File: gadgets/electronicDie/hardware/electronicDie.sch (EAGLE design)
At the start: 32 parts, among them IC1 CD4029N, IC2 NE555N, T1 BC327, T2 BC337, X1 USBPCB

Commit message: Add SMD power LED for testing purposes
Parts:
- added LED8: green, led:LEDCHIPLED_0603
- added R11: 1k, rcl_upravena:R-EU_R0603
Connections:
- new net N$3: LED8.A, R11.1
- net +5V: now also R11.2
- net GND: now also LED8.C
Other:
- moved on the sheet: C1, C2, C3, C4, D1, D2, D3, IC1, IC1P, IC2, LED1, LED2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

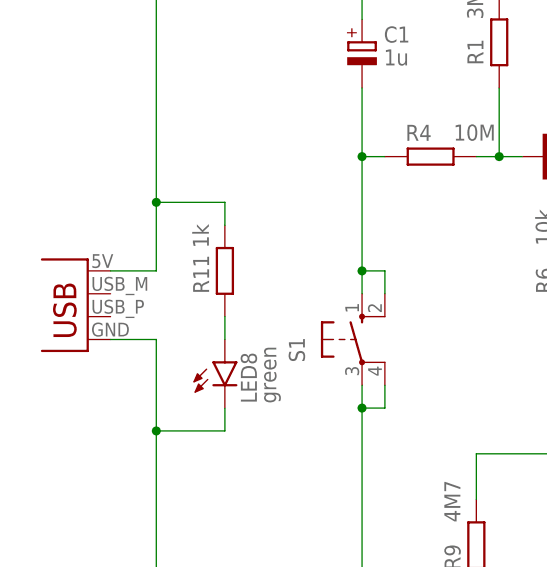
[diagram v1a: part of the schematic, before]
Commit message: Add NC symbol to USB data pins
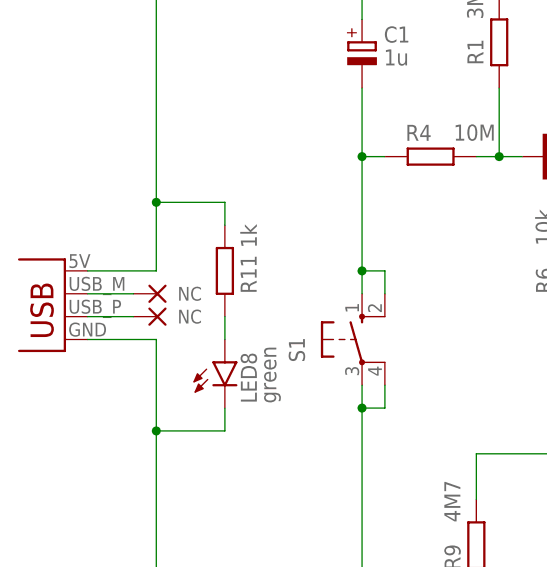
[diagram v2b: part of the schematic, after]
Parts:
- added NC3, NC4: NC, NC:NC
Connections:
- new net N$23: NC3.NC, X1.D-
- new net N$24: NC4.NC, X1.D+
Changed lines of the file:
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@@
 <part name="LED8" library="led" deviceset="LED" device="CHIPLED_0603" package3d_urn="urn:adsk.eagle:package:15822/2" value="green"/>
 <part name="R11" library="rcl_upravena" deviceset="R-EU_" device="R0603" value="1k"/>
+<part name="NC3" library="NC" deviceset="NC" device=""/>
+<part name="NC4" library="NC" deviceset="NC" device=""/>
 </parts>
 <sheets>
@@
 <attribute name="VALUE" x="190.5" y="121.3866" size="1.778" layer="96"/>
 </instance>
-<instance part="X1" gate="G$1" x="22.86" y="93.98" smashed="yes" rot="MR0"/>
+<instance part="X1" gate="G$1" x="20.32" y="93.98" smashed="yes" rot="MR0"/>
 <instance part="C2" gate="G$1" x="106.68" y="121.92" smashed="yes" rot="MR0">
 <attribute name="NAME" x="104.14" y="122.047" size="1.778" layer="95" rot="MR0"/>
@@
 <attribute name="VALUE" x="43.815" y="86.868" size="1.778" layer="96" rot="R90"/>
 </instance>
-<instance part="R11" gate="G$1" x="38.1" y="101.6" smashed="yes" rot="R90">
-<attribute name="NAME" x="36.3474" y="99.06" size="1.778" layer="95" rot="R90"/>
-<attribute name="VALUE" x="36.322" y="104.14" size="1.778" layer="96" rot="R90"/>
-</instance>
+<instance part="R11" gate="G$1" x="38.1" y="101.6" smashed="yes" rot="MR90">
+<attribute name="NAME" x="39.8526" y="99.06" size="1.778" layer="95" rot="MR90"/>
+<attribute name="VALUE" x="39.878" y="104.14" size="1.778" layer="96" rot="MR90"/>
+</instance>
+<instance part="NC3" gate="G$1" x="27.94" y="99.06" smashed="yes"/>
+<instance part="NC4" gate="G$1" x="27.94" y="96.52" smashed="yes"/>
 </instances>
 <busses>
@@
 <junction x="53.34" y="86.36"/>
 <pinref part="X1" gate="G$1" pin="GND"/>
-<wire x1="25.4" y1="93.98" x2="30.48" y2="93.98" width="0.1524" layer="91"/>
+<wire x1="22.86" y1="93.98" x2="30.48" y2="93.98" width="0.1524" layer="91"/>
 <wire x1="30.48" y1="93.98" x2="30.48" y2="83.82" width="0.1524" layer="91"/>
 <wire x1="30.48" y1="83.82" x2="30.48" y2="60.96" width="0.1524" layer="91"/>
@@
 <junction x="200.66" y="137.16"/>
 <pinref part="X1" gate="G$1" pin="VBUS"/>
-<wire x1="25.4" y1="101.6" x2="30.48" y2="101.6" width="0.1524" layer="91"/>
+<wire x1="22.86" y1="101.6" x2="30.48" y2="101.6" width="0.1524" layer="91"/>
 <wire x1="30.48" y1="101.6" x2="30.48" y2="109.22" width="0.1524" layer="91"/>
 <wire x1="30.48" y1="109.22" x2="30.48" y2="137.16" width="0.1524" layer="91"/>
@@
 </segment>
 </net>
+<net name="N$23" class="0">
+<segment>
+<pinref part="X1" gate="G$1" pin="D-"/>
+<pinref part="NC3" gate="G$1" pin="NC"/>
+<wire x1="22.86" y1="99.06" x2="27.94" y2="99.06" width="0.1524" layer="91"/>
+</segment>
+</net>
+<net name="N$24" class="0">
+<segment>
+<pinref part="X1" gate="G$1" pin="D+"/>
+<pinref part="NC4" gate="G$1" pin="NC"/>
+<wire x1="22.86" y1="96.52" x2="27.94" y2="96.52" width="0.1524" layer="91"/>
+</segment>
+</net>

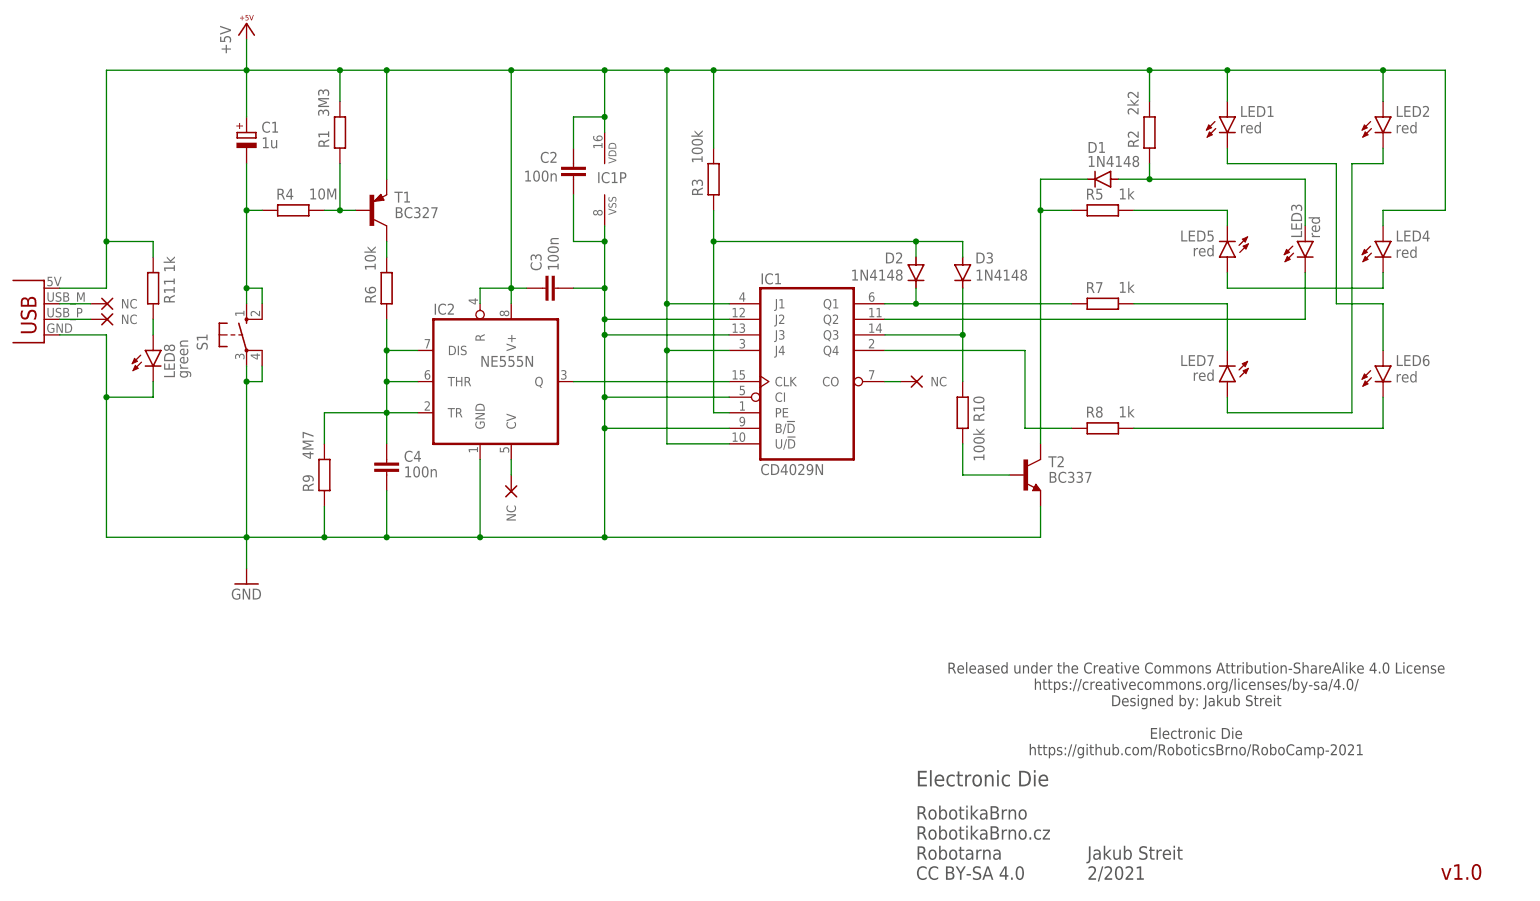
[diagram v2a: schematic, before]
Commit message: ElectronicDie: fix v1.0 problems - make it bigger - change resistors and diodes package size - make larger spaces between parts - minimize part types - fix PNP transistor pinout - remove SMD power LED
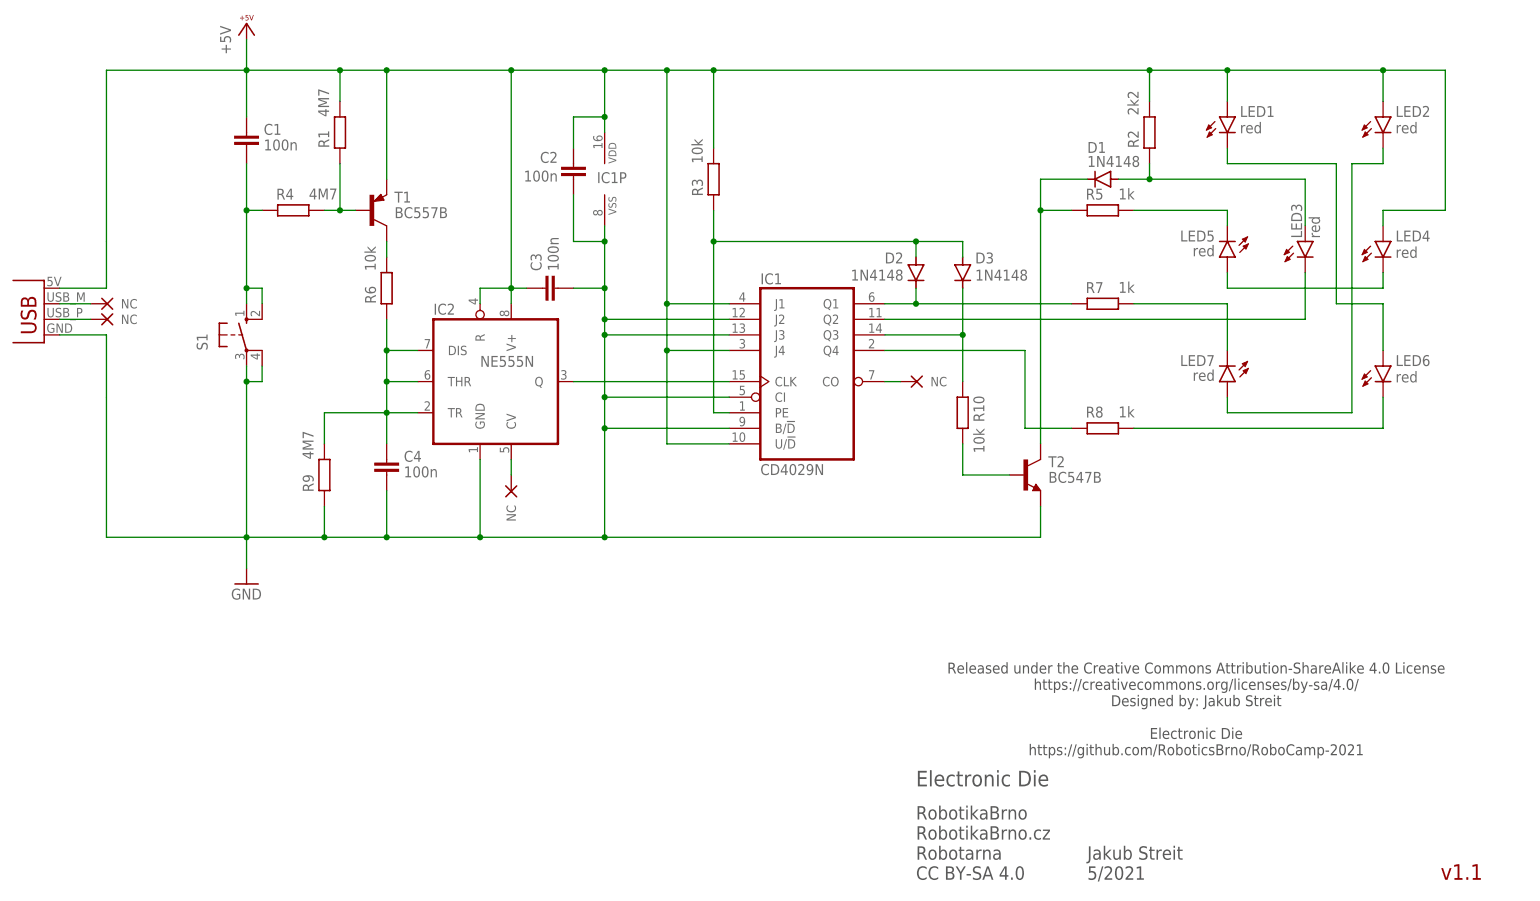
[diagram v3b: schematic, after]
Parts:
- removed LED8: green, led:LEDCHIPLED_0603
- removed R11: 1k, rcl_upravena:R-EU_R0603
- C1: value 1u -> 100n; device rcl_upravena:CPOL-EUE2-5 -> rcl_upravena:C-EU050-024X044
- C2, C3, C4: device rcl_upravena:C-EU025-025X050 -> rcl_upravena:C-EU050-024X044
- D1, D2, D3: device diode:1N4148DO35-7 -> diode:1N4148DO35-10
- R1: value 3M3 -> 4M7; device rcl_upravena:R-EU_0204/7 -> rcl_upravena:R-EU_0207/12
- R10, R3: value 100k -> 10k; device rcl_upravena:R-EU_0204/7 -> rcl_upravena:R-EU_0207/12
- R2, R5, R6, R7, R8, R9: device rcl_upravena:R-EU_0204/7 -> rcl_upravena:R-EU_0207/12
- R4: value 10M -> 4M7; device rcl_upravena:R-EU_0204/7 -> rcl_upravena:R-EU_0207/12
- T1: value BC327 -> BC557B; device transistor:BC327-16-PNP-TO92-EBC -> transistor:2N4126-PNP-TO92-CBE
- T2: value BC337 -> BC547B
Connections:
- removed net N$3: LED8.A, R11.1
- net +5V: now also C1.1; no longer C1.+, R11.2
- net GND: no longer LED8.C
- net N$1: now also C1.2; no longer C1.-
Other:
- note added: "Jakub Streit 5/2021"
- note added: "v1.1"
- note removed: "Jakub Streit 2/2021"
- note removed: "v1.0"

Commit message: ElectronicDie v1.2: more resistant to assembly errors - resistors with same value grouped together - diodes grouped together - larger spaces between parts - 2k2 resistor replaced with 2 × 1k (so only 3 types of resistors left: 1k, 10k and 4M7) - added parts value to silkscreen - URL in silkscreen changed from robotikabrno.cz to robotickytabor.cz - changed year of Robocamp to 2022 (but 2021 remains in repo URL) - added silkscreen label for engraving owner name
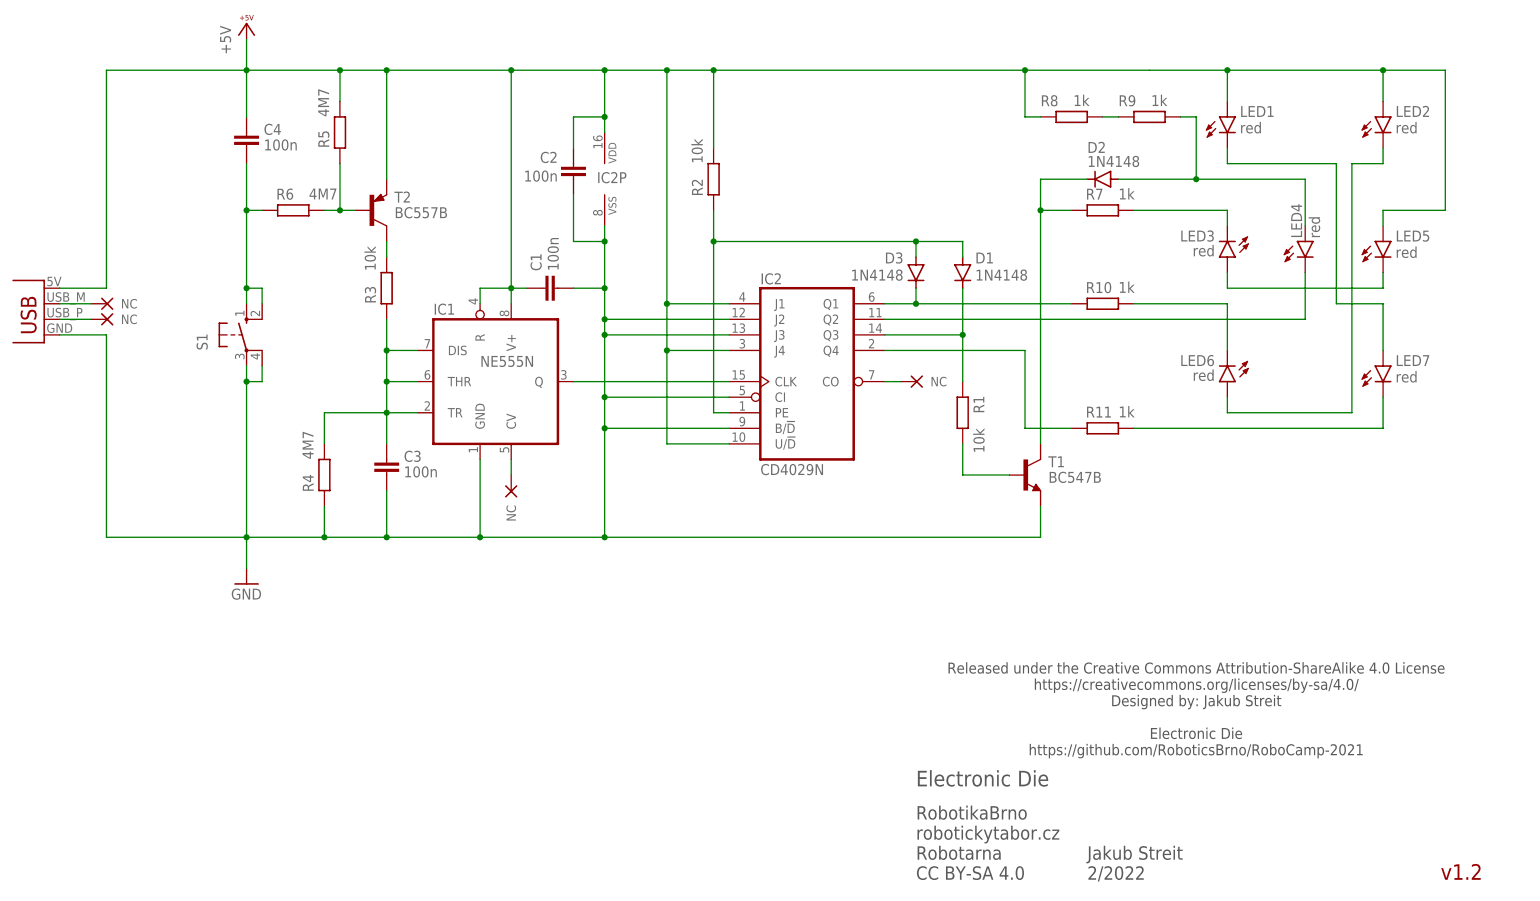
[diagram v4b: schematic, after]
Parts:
- added R11: 1k, rcl_upravena:R-EU_0207/12
- IC1: value CD4029N -> NE555N; device 40xx:4029N -> 555:NE555N
- IC2: value NE555N -> CD4029N; device 555:NE555N -> 40xx:4029N
- R1: value 4M7 -> 10k
- R10: value 10k -> 1k
- R2: value 2k2 -> 10k
- R5: value 1k -> 4M7
- R6: value 10k -> 4M7
- R9: value 4M7 -> 1k
- T1: value BC557B -> BC547B; device transistor:2N4126-PNP-TO92-CBE -> transistor:BC337-16-NPN-TO92-CBE
- T2: value BC547B -> BC557B; device transistor:BC337-16-NPN-TO92-CBE -> transistor:2N4126-PNP-TO92-CBE
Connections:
- new net N$3: R8.1, R9.2
- net +5V: now also C4.1, IC1.R, IC1.V+, IC2A.J1, IC2A.J4, IC2A.U/!D, IC2P.VDD, LED5.A, R5.2, R8.2, T2.E; no longer C3.1, IC1A.J1, IC1A.J4, IC1A.U/!D, IC1P.VDD, IC2.R, IC2.V+, LED4.A, R1.2, R3.2, T1.E
- net GND: now also C1.2, IC1.GND, IC2A.B/!D, IC2A.CI, IC2A.J2, IC2A.J3, IC2P.VSS, R4.1, T1.E; no longer C4.2, IC1A.B/!D, IC1A.CI, IC1A.J2, IC1A.J3, IC1P.VSS, IC2.GND, R9.1, T2.E
- net N$1: now also C4.2, R6.1; no longer C1.2, R4.1
- net N$10: now also D3.C, IC2A.Q1, R10.1; no longer D2.C, IC1A.Q1, R7.1
- net N$11: now also D1.C, IC2A.Q3, R1.1; no longer D3.C, IC1A.Q3, R10.1
- net N$12: now also IC2A.Q4, R11.1; no longer IC1A.Q4, R8.1
- net N$13: now also LED3.A, LED5.C; no longer LED4.C, LED5.A
- net N$14: now also LED6.A; no longer LED7.A
- net N$15: now also IC2A.CO; no longer IC1A.CO
- net N$16: now also LED7.A; no longer LED6.A
- net N$17: now also R1.2, T1.B; no longer R10.2, T2.B
- net N$18: now also LED3.C, R7.2; no longer LED5.C, R5.2
- net N$19: now also D2.A, LED4.A, R9.1; no longer D1.A, LED3.A, R2.1
- net N$2: now also R5.1, R6.2, T2.B; no longer R1.1, R4.2, T1.B
- net N$20: now also IC2A.Q2, LED4.C; no longer IC1A.Q2, LED3.C
- net N$21: now also D2.C, R7.1, T1.C; no longer D1.C, R5.1, T2.C
- net N$22: now also LED7.C, R11.2; no longer LED6.C, R8.2
- net N$4: now also R3.2, T2.C; no longer R6.2, T1.C
- net N$5: now also C3.1, IC1.DIS, IC1.THR, IC1.TR, R3.1, R4.2; no longer C4.1, IC2.DIS, IC2.THR, IC2.TR, R6.1, R9.2
- net N$6: now also IC1.CV; no longer IC2.CV
- net N$7: now also IC1.Q, IC2A.CLK; no longer IC1A.CLK, IC2.Q
- net N$8: now also LED6.C, R10.2; no longer LED7.C, R7.2
- net N$9: now also D1.A, IC2A.PE, R2.1; no longer D2.A, IC1A.PE, R3.1
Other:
- note added: "Jakub Streit 2/2022"
- note added: "RobotikaBrno robotickytabor.cz Robotarna CC BY-SA 4.0"
- note added: "v1.2"
- note removed: "Jakub Streit 5/2021"
- note removed: "RobotikaBrno RobotikaBrno.cz Robotarna CC BY-SA 4.0"
- note removed: "v1.1"
- moved on the sheet: C1, C3, C4, D1, D2, D3, LED3, LED4, LED5, LED6, LED7, R1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
